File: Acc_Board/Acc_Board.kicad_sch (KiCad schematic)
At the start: 37 parts, among them J1 1053091202, J2 1053091202, J4 1053091202, J5 1053091202, J6 1053091202, K1 Relay_SPST-NO, K7 Latching Relay, Q1 Q_NMOS_SDG, U1 NUCLEO-L432KC, U11 DK1A1B-12V, U13 NAND, U14 LM555N, U2 L7805CV, U2 NSL-32, U3 PQDE6W-Q110-S5-H-D, U4 ISO1050DUB, U5 LTC6820HMS-TRPBF, U6 DK1A1B-12V

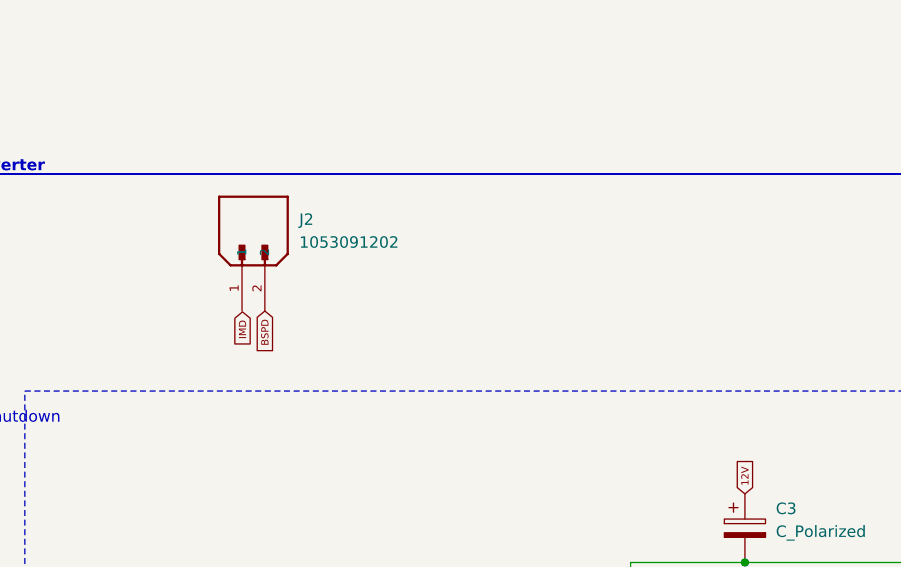
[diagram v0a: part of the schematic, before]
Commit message: Added labels for ACC board
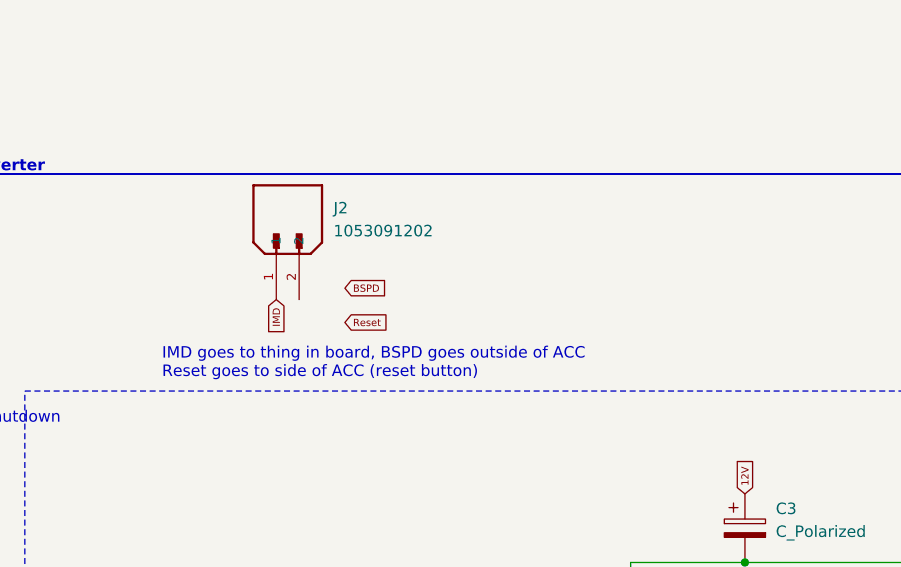
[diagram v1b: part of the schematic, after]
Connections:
- net BSPD: no longer J2.2
- net IMD: now also J2.1
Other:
- note added: "IMD goes to thing in board, BSPD goes outside of ACC Reset goes to side of ACC (reset button)"
- moved on the sheet: J2
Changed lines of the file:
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@@
     (effects (font (size 1.27 1.27) (thickness 0.254) bold) (justify left bottom))
+  )
+  (text "IMD goes to thing in board, BSPD goes outside of ACC\nReset goes to side of ACC (reset button)"
+    (at 264.16 73.66 0)
+    (effects (font (size 1.27 1.27)) (justify left bottom))
   )
   (text "DCDC converter" (at 235.585 50.8 0)
@@
     )
   )
+  (global_label "Reset" (shape input) (at 284.48 67.31 0) (fields_autoplaced)
+    (effects (font (size 0.8 0.8) (color 72 72 72 1)) (justify left))
+    (property "Intersheetrefs" "${INTERSHEET_REFS}" (at 289.6364 67.31 0)
+      (effects (font (size 1.27 1.27)) (justify left) hide)
+    )
+  )
   (global_label "GND" (shape input) (at 377.19 106.553 0) (fields_autoplaced)
     (effects (font (size 0.8 0.8) (color 0 0 0 1)) (justify left))
@@
     )
   )
-  (global_label "BSPD" (shape input) (at 275.59 66.04 270) (fields_autoplaced)
-    (effects (font (size 0.8 0.8) (color 72 72 72 1)) (justify right))
-    (property "Intersheetrefs" "${INTERSHEET_REFS}" (at 275.59 71.0822 90)
-      (effects (font (size 1.27 1.27)) (justify right) hide)
+  (global_label "BSPD" (shape input) (at 284.48 63.5 0) (fields_autoplaced)
+    (effects (font (size 0.8 0.8) (color 72 72 72 1)) (justify left))
+    (property "Intersheetrefs" "${INTERSHEET_REFS}" (at 289.5222 63.5 0)
+      (effects (font (size 1.27 1.27)) (justify left) hide)
     )
   )
@@
     )
   )
-  (global_label "IMD" (shape input) (at 273.1054 66.1356 270) (fields_autoplaced)
+  (global_label "IMD" (shape input) (at 276.86 64.77 270) (fields_autoplaced)
     (effects (font (size 0.8 0.8) (color 72 72 72 1)) (justify right))
-    (property "Intersheetrefs" "${INTERSHEET_REFS}" (at 273.1054 70.1112 90)
+    (property "Intersheetrefs" "${INTERSHEET_REFS}" (at 276.86 68.7456 90)
       (effects (font (size 1.27 1.27)) (justify right) hide)
     )
@@
     )
   )
-  (symbol (lib_id "molex_1053091202:1053091202") (at 273.05 60.96 90) (unit 1)
+  (symbol (lib_id "molex_1053091202:1053091202") (at 276.86 59.69 90) (unit 1)
     (in_bom yes) (on_board yes) (dnp no) (fields_autoplaced)
-    (property "Reference" "J2" (at 279.4 55.88 90)
+    (property "Reference" "J2" (at 283.21 54.61 90)
       (effects (font (size 1.27 1.27)) (justify right))
     )
-    (property "Value" "1053091202" (at 279.4 58.42 90)
+    (property "Value" "1053091202" (at 283.21 57.15 90)
       (effects (font (size 1.27 1.27)) (justify right))
     )
-    (property "Footprint" "1FS_2_Global_Footprint_Library:MOLEX_1053091202" (at 273.05 60.96 0)
+    (property "Footprint" "1FS_2_Global_Footprint_Library:MOLEX_1053091202" (at 276.86 59.69 0)
       (effects (font (size 1.27 1.27)) (justify bottom) hide)
     )
-    (property "Datasheet" "" (at 273.05 60.96 0)
-      (effects (font (size 1.27 1.27)) hide)
-    )
-    (property "PARTREV" "H" (at 273.05 60.96 0)
+    (property "Datasheet" "" (at 276.86 59.69 0)
+      (effects (font (size 1.27 1.27)) hide)
+    )
+    (property "PARTREV" "H" (at 276.86 59.69 0)
       (effects (font (size 1.27 1.27)) (justify bottom) hide)
     )
-    (property "STANDARD" "Manufacturer Recommendations" (at 273.05 60.96 0)
+    (property "STANDARD" "Manufacturer Recommendations" (at 276.86 59.69 0)
       (effects (font (size 1.27 1.27)) (justify bottom) hide)
     )
-    (property "MAXIMUM_PACKAGE_HEIGHT" "10.51 mm" (at 273.05 60.96 0)
+    (property "MAXIMUM_PACKAGE_HEIGHT" "10.51 mm" (at 276.86 59.69 0)
       (effects (font (size 1.27 1.27)) (justify bottom) hide)
     )
-    (property "MANUFACTURER" "Molex" (at 273.05 60.96 0)
+    (property "MANUFACTURER" "Molex" (at 276.86 59.69 0)
       (effects (font (size 1.27 1.27)) (justify bottom) hide)
     )

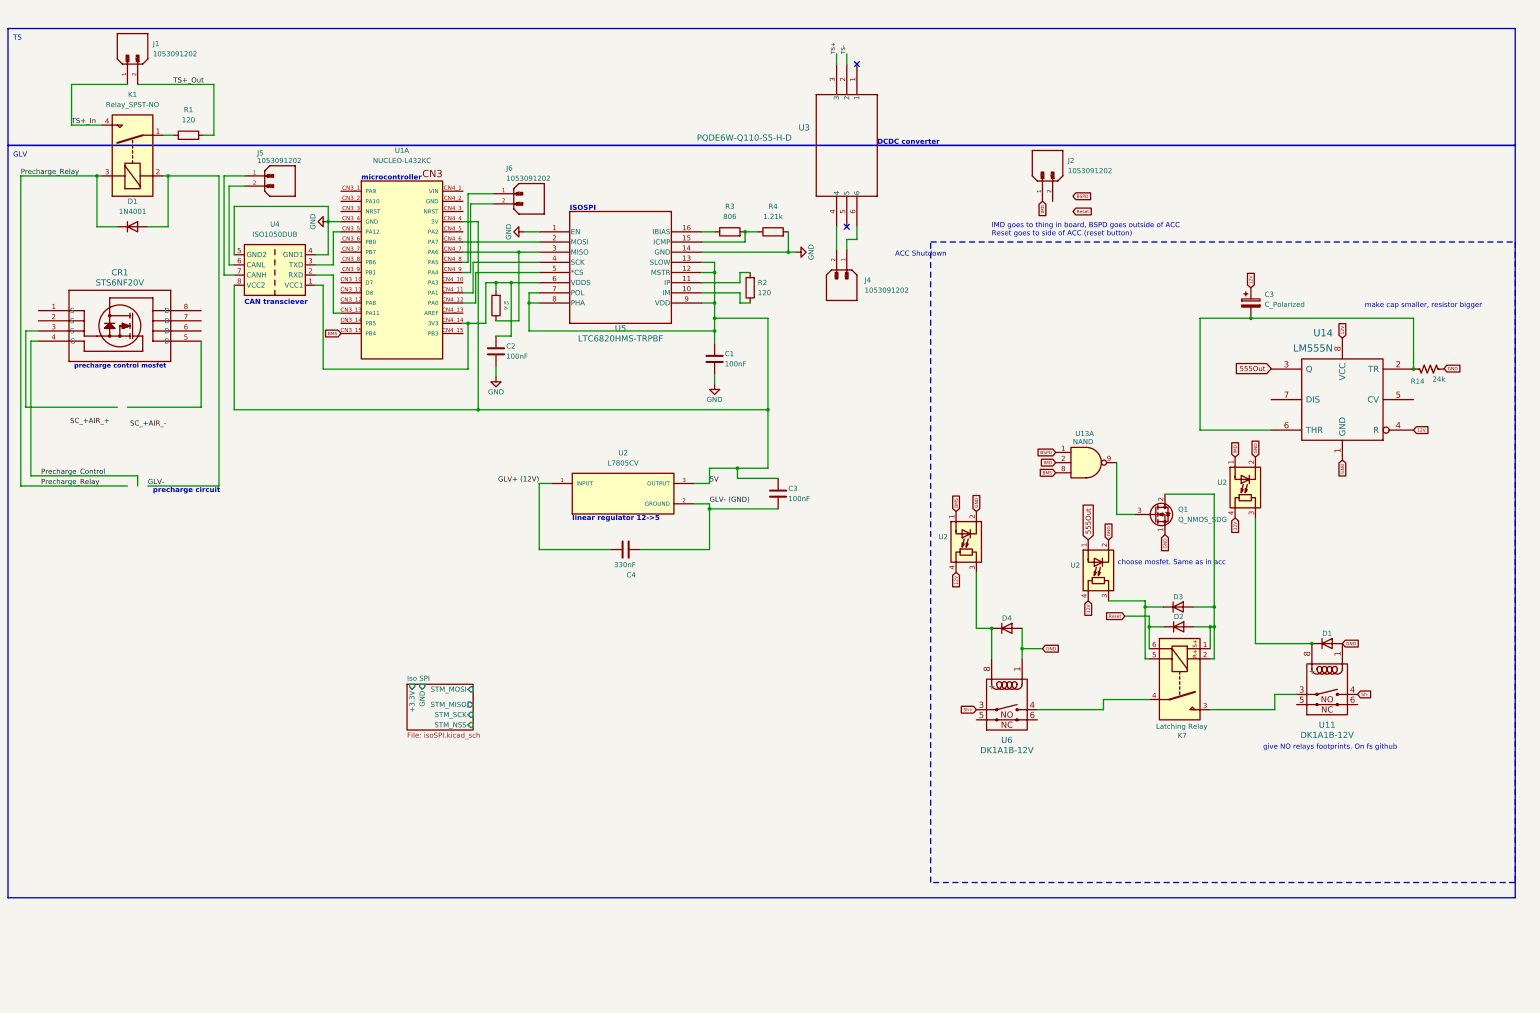
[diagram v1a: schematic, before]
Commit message: Removed ACC parts from BSPD board and organized ACC board schematic
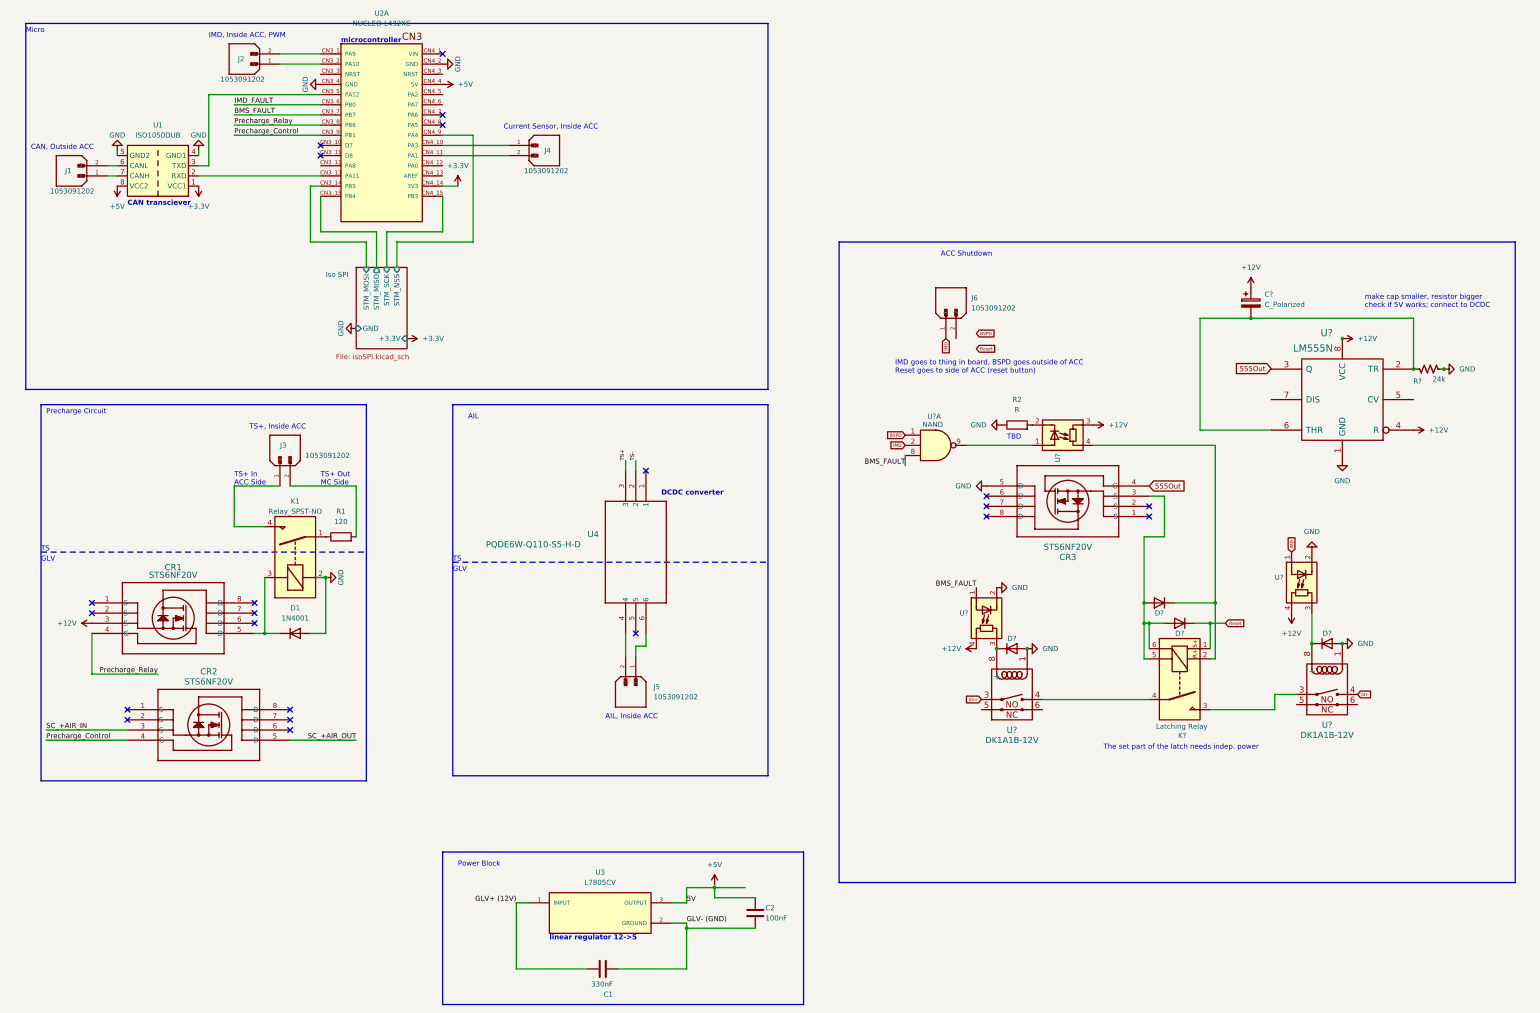
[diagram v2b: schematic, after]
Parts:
- removed C1, C2: 100nF, 1FS_2_Global_Footprint_Library:Basic 2 Hole, symbol Device:C
- removed J6: 1053091202, 1FS_2_Global_Footprint_Library:MOLEX_1053091202, symbol molex_1053091202:1053091202
- removed Q1: Q_NMOS_SDG, 1FS_2_Global_Footprint_Library:SO-8_STM, symbol Device:Q_NMOS_SDG
- removed R3: 806, Resistor_THT:R_Axial_DIN0207_L6.3mm_D2.5mm_P10.16mm_Horizontal, symbol Device:R
- removed R4: 1.21k, Resistor_THT:R_Axial_DIN0207_L6.3mm_D2.5mm_P10.16mm_Horizontal, symbol Device:R
- removed R5: 2k, Resistor_THT:R_Axial_DIN0207_L6.3mm_D2.5mm_P10.16mm_Horizontal, symbol Device:R
- removed U2: NSL-32, 1FS_2_Global_Footprint_Library:OptoCoupler 6-SOP, symbol Isolator:NSL-32
- removed U5: LTC6820HMS-TRPBF, 1FS_2_Global_Footprint_Library:MS_05-08-1669_ADI, symbol 1_ACC_BOARD:LTC6820HMS-TRPBF
- added CR1, CR3: STS6NF20V, 1FS_2_Global_Footprint_Library:SO-8_STM, symbol 1_ACC_BOARD:STS6NF20V
- added J2, J4: 1053091202, 1FS_2_Global_Footprint_Library:MOLEX_1053091202, symbol molex_1053091202:1053091202
- added U?: NSL-32, 1FS_2_Global_Footprint_Library:OptoCoupler 6-SOP, symbol Isolator:NSL-32
- R1: footprint Resistor_THT:R_Axial_DIN0207_L6.3mm_D2.5mm_P10.16mm_Horizontal -> 1FS_2_Global_Footprint_Library:THS15120RJ
- R2: value 120 -> R; footprint Resistor_THT:R_Axial_DIN0207_L6.3mm_D2.5mm_P10.16mm_Horizontal -> (none)
- U2: renamed from U1; footprint NUCLEO-L432KC:MODULE_NUCLEO-L432KC -> 1FS_2_Global_Footprint_Library:MODULE_NUCLEO-L432KC
- renumbered C4 to C1, C3 to C2, C3 to C?, CR1 to CR2, D1 to D?, D3 to D?, D2 to D?, D4 to D?, J5 to J1, J1 to J3, J4 to J5, J2 to J6, K7 to K?, R14 to R?, U4 to U1, U2 to U3, U3 to U4, U11 to U?, U2 to U?, U13 to U?, U6 to U?, U14 to U?
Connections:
- net GLV- is gone; now on net GND: D1.2 (A), K1.2
- net 555Out: now also CR3.4 (G)
- net 5V: no longer U1.8 (VCC2), U2.CN4_4 (5V)
- net GND: now also R2.1, U2.CN4_2 (GND), CR3.5 (D)
- net Iso SPI/STM_MISO: now also U2.CN3_15 (PB4)
- net Iso SPI/STM_MOSI: now also U2.CN3_14 (PB5)
- net Iso SPI/STM_NSS: now also U2.CN4_9 (PA4)
- net Iso SPI/STM_SCK: now also U2.CN4_15 (PB3)
- net Precharge_Control: now also U2.CN3_9 (PB1)
- net Precharge_Relay: now also U2.CN3_8 (PB6), CR1.4 (G); no longer D1.1 (K), K1.3
- net Reset: now also K?.1; no longer K?.6
- net +3.3V: now reaches U1.1 (VCC1), U2.CN4_14 (3V3)
- net at R2.2: now also U?.2 (K)
- net at U2.CN4_11 (PA1): now also J4.2
- net at D?.1 (K): now also K?.2, U?.4 (R); no longer K?.5
- net at D?.2 (A), D?.2 (A): now also K?.5, K?.6, CR3.3 (S); no longer K?.1, K?.2
- net at U?.9: now also U?.1 (A)
- net SC_+AIR_IN: now reaches CR2.3 (S)
- net SC_+AIR_OUT: now reaches CR2.5 (D)
- net at U2.CN3_1 (PA9): now also J2.2
- net at U2.CN3_2 (PA10): now also J2.1
- net IMD_FAULT: now reaches U2.CN3_6 (PB0)
- net BMS_FAULT: now reaches U2.CN3_7 (PB7)
- net BMS_FAULT: now also U?.1 (A), U?.8
- net at U2.CN4_10 (PA3): now also J4.1
- net 12V renamed +12V
- net +12V: now also CR1.3 (S), U?.3 (R)
- removed net BMS: U2.CN3_15 (PB4), U?.1 (A), U?.8
- net TS+_In: no longer names the net of J3.1, K1.4
- net TS+_Out: no longer names the net of J3.2, R1.+
- new net: CR1.5 (D), D1.1 (K), K1.3
- new net +5V: U1.8 (VCC2), U2.CN4_4 (5V)
- no-connect marks 2 -> 22
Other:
- note added: "AIL"
- note added: "AIL, Inside ACC"
- note added: "CAN, Outside ACC"
- note added: "Current Sensor, Inside ACC"
- note added: "IMD, Inside ACC, PWM"
- note added: "Micro"
- note added: "Power Block"
- note added: "Precharge Circuit"
- note added: "TBD"
- note added: "TS+ In ACC Side"
- note added: "TS+ Out MC Side"
- note added: "TS+, Inside ACC"
- note added: "The set part of the latch needs indep. power"
- note added: "make cap smaller, resistor bigger check if 5V works; connect to DCDC"
- note removed: "ISOSPI"
- note removed: "choose mosfet. Same as in acc"
- note removed: "give NO relays footprints. On fs github"
- note removed: "make cap smaller, resistor bigger"
- note removed: "precharge circuit"
- note removed: "precharge control mosfet"
- company: (none) -> Formula Slug
- title: (none) -> Accumulator Board
- moved on the sheet: C1, C2, CR2, D1, D?, J1, J3, J5, J6, K1, R1, U1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
